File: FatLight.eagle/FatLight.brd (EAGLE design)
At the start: 75 x 100 mm, 27 parts, among them Q1 IRF540, Q2 IRF540, Q3 IRF540, Q4 16MHz, U1 ATMEGA328P-PU

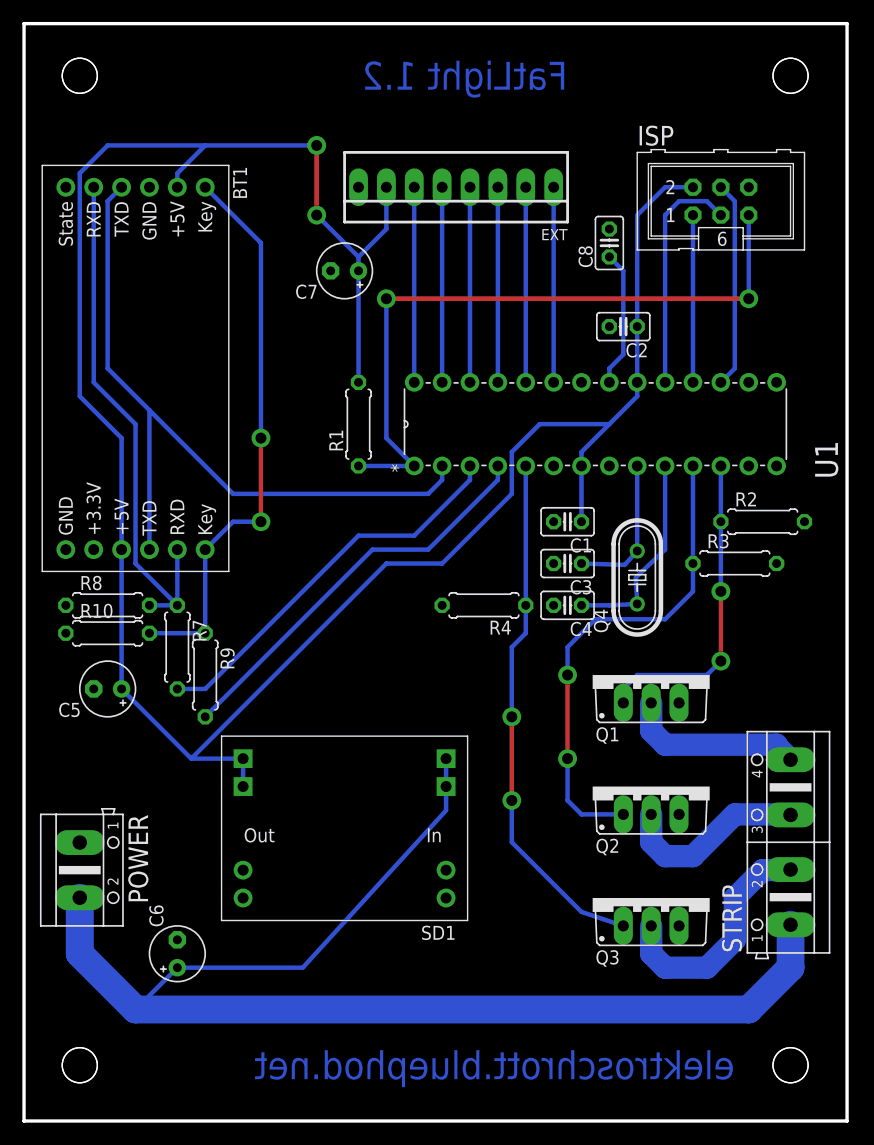
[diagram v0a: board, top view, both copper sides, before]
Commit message: Neue Board-Revision 1.3 mit stark optimiertem Layout und korrigiertem BT-Pinout
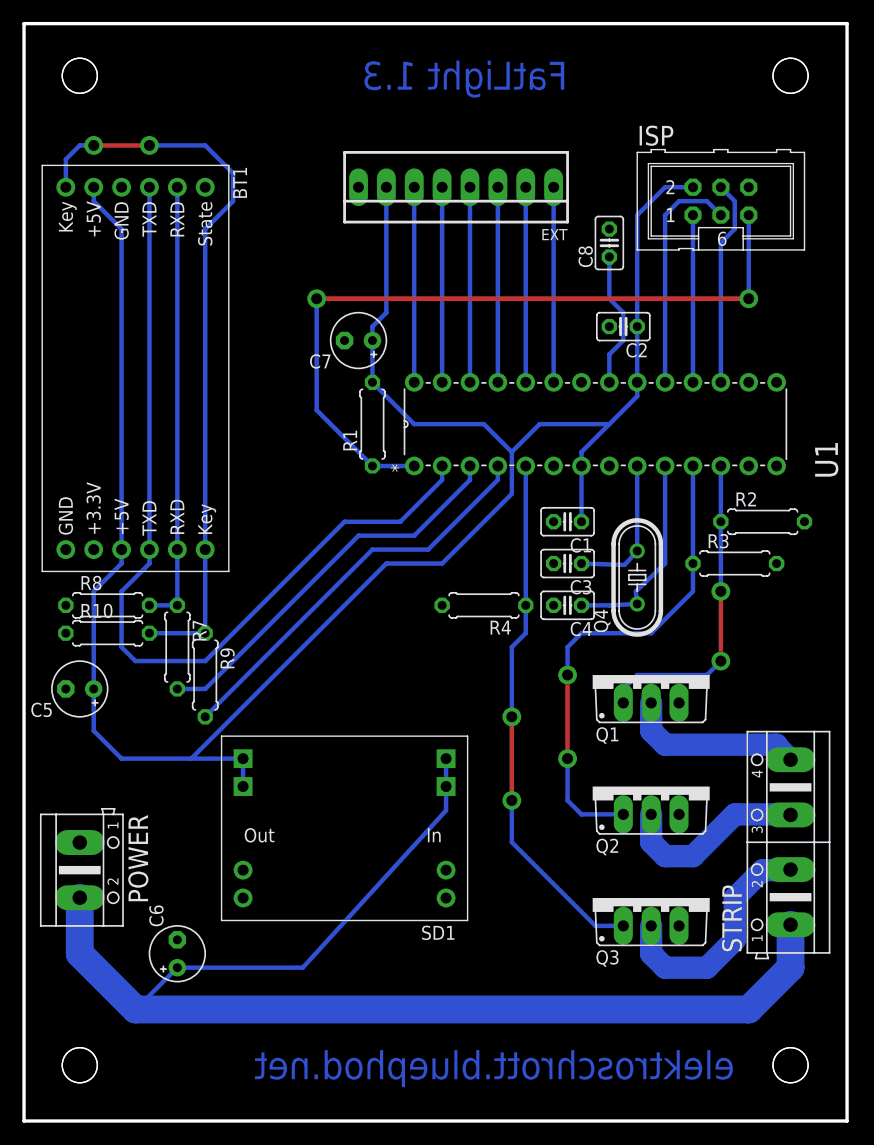
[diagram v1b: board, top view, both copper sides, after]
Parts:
- moved C7 6.48 mm to (30.5, 71.1)
- moved C5 2.54 mm to (5.08, 39.4)
- moved R1 1.27 mm to (31.8, 63.5)
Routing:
- net +5V: track 212.0 -> 191.6 mm, vias 2 -> 0
- net N$3: track 51.4 -> 67.4 mm
- net RXD_MCU: track 66.7 -> 80.8 mm
- net N$4: track 48.9 -> 40.6 mm
- net RESET: track 62.0 -> 68.1 mm
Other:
- board text added: "FatLight 1.3"
- board text removed: "FatLight 1.2"

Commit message: Bestückungsdruck verbessert
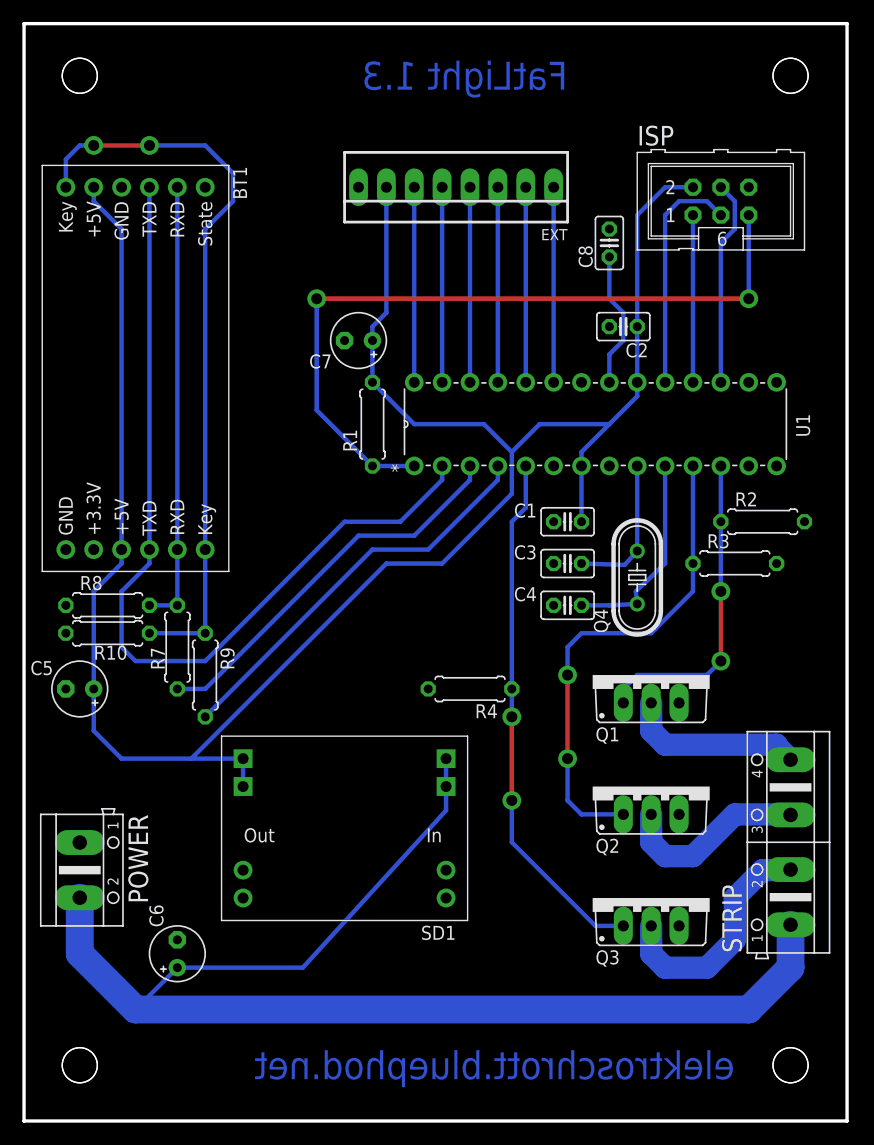
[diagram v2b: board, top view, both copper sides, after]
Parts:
- moved R4 7.73 mm to (40.6, 39.4)
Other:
- board text added: "+12/B/G/R"
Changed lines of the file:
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@@
 <text x="49.53" y="93.98" size="2.54" layer="16" font="vector" ratio="15" rot="MR0">FatLight 1.3</text>
 <text x="64.77" y="3.81" size="2.54" layer="16" font="vector" ratio="15" rot="MR0">elektroschrott.bluephod.net</text>
+<text x="65.405" y="24.765" size="1.27" layer="27" rot="R90">+12/B/G/R</text>
 </plain>
 <attributes>
@@
 </autorouter>
 <elements>
-<element name="BT1" library="ZAP-Wireless" package="HC-05-6PIN" value="BT-MODULE" x="10.16" y="68.58" rot="R270"/>
-<element name="C1" library="rcl" package="C025-025X050" value="100nF" x="49.53" y="54.61" rot="R180"/>
+<element name="BT1" library="ZAP-Wireless" package="HC-05-6PIN" value="BT-MODULE" x="10.16" y="68.58" smashed="yes" rot="R270">
+<attribute name="NAME" x="19.05" y="86.995" size="1.27" layer="21" rot="R270"/>
+<attribute name="VALUE" x="3.81" y="74.295" size="1.27" layer="27" rot="R270"/>
+</element>
+<element name="C1" library="rcl" package="C025-025X050" value="100nF" x="49.53" y="54.61" smashed="yes" rot="R180">
+<attribute name="NAME" x="46.736" y="56.261" size="1.27" layer="25" ratio="10" rot="R180"/>
+<attribute name="VALUE" x="46.736" y="54.864" size="1.27" layer="27" ratio="10" rot="R180"/>
+</element>
 <element name="C2" library="rcl" package="C025-025X050" value="100nF" x="54.61" y="72.39" rot="R180"/>
-<element name="C3" library="rcl" package="C025-025X050" value="22pF" x="49.53" y="50.8" rot="R180"/>
-<element name="C4" library="rcl" package="C025-025X050" value="22pF" x="49.53" y="46.99" rot="R180"/>
-<element name="C5" library="rcl" package="E2,5-5" value="100µF" x="5.08" y="39.37" rot="R180"/>
+<element name="C3" library="rcl" package="C025-025X050" value="22pF" x="49.53" y="50.8" smashed="yes" rot="R180">
+<attribute name="NAME" x="46.736" y="52.451" size="1.27" layer="25" ratio="10" rot="R180"/>
+<attribute name="VALUE" x="46.736" y="51.054" size="1.27" layer="27" ratio="10" rot="R180"/>
+</element>
+<element name="C4" library="rcl" package="C025-025X050" value="22pF" x="49.53" y="46.99" smashed="yes" rot="R180">
+<attribute name="NAME" x="46.736" y="48.641" size="1.27" layer="25" ratio="10" rot="R180"/>
+<attribute name="VALUE" x="46.736" y="47.244" size="1.27" layer="27" ratio="10" rot="R180"/>
+</element>
+<element name="C5" library="rcl" package="E2,5-5" value="100µF" x="5.08" y="39.37" smashed="yes" rot="R180">
+<attribute name="NAME" x="2.667" y="41.91" size="1.27" layer="25" ratio="10" rot="R180"/>
+<attribute name="VALUE" x="1.397" y="38.227" size="1.27" layer="27" ratio="10" rot="R270"/>
+</element>
 <element name="C6" library="rcl" package="E2,5-5" value="100µF" x="13.97" y="15.24" rot="R90"/>
 <element name="EXT" library="con-molex" package="22-23-2081" value="PSK-8" x="39.37" y="85.09" rot="R180">
@@
 </element>
 <element name="R1" library="rcl" package="0207/7" value="10k" x="31.75" y="63.5" rot="R90"/>
-<element name="R10" library="rcl" package="0207/7" value="20k" x="7.62" y="44.45"/>
+<element name="R10" library="rcl" package="0207/7" value="20k" x="7.62" y="44.45" smashed="yes">
+<attribute name="NAME" x="6.35" y="42.037" size="1.27" layer="25" ratio="10"/>
+<attribute name="VALUE" x="5.334" y="43.8912" size="1.27" layer="27" ratio="10"/>
+</element>
 <element name="R2" library="rcl" package="0207/7" value="10k" x="67.31" y="54.61"/>
 <element name="R3" library="rcl" package="0207/7" value="10k" x="64.77" y="50.8"/>
-<element name="R4" library="rcl" package="0207/7" value="10k" x="41.91" y="46.99" rot="R180"/>
-<element name="R7" library="rcl" package="0207/7" value="10k" x="13.97" y="43.18" rot="R270"/>
+<element name="R4" library="rcl" package="0207/7" value="10k" x="40.64" y="39.37" rot="R180"/>
+<element name="R7" library="rcl" package="0207/7" value="10k" x="13.97" y="43.18" smashed="yes" rot="R270">
+<attribute name="NAME" x="11.557" y="43.18" size="1.27" layer="25" ratio="10" rot="R270"/>
+<attribute name="VALUE" x="13.4112" y="45.466" size="1.27" layer="27" ratio="10" rot="R270"/>
+</element>
 <element name="R8" library="rcl" package="0207/7" value="20k" x="7.62" y="46.99"/>
 <element name="R9" library="rcl" package="0207/7" value="10k" x="16.51" y="40.64" rot="R270"/>
-<element name="SD1" library="Zap-Powerconverters" package="STEPDOWN-21X16" value="D-SUN-STEPDOWN" x="29.21" y="26.67" rot="R180"/>
-<element name="U1" library="Zap-Mikrocontroller" package="DIP254P762X457-28" value="ATMEGA328P-PU" x="68.58" y="67.31" rot="R90">
+<element name="SD1" library="Zap-Powerconverters" package="STEPDOWN-21X16" value="D-SUN-STEPDOWN" x="29.21" y="26.67" smashed="yes" rot="R180">
+<attribute name="NAME" x="39.37" y="17.78" size="1.27" layer="25" rot="R180"/>
+<attribute name="VALUE" x="37.465" y="28.575" size="1.27" layer="27" rot="R180"/>
+</element>
+<element name="U1" library="Zap-Mikrocontroller" package="DIP254P762X457-28" value="ATMEGA328P-PU" x="68.58" y="67.31" smashed="yes" rot="R90">
 <attribute name="PACKAGE" value="PDIP-28" x="68.58" y="67.31" size="1.778" layer="27" rot="R90" display="off"/>
 <attribute name="OC_NEWARK" value="15R0268" x="68.58" y="67.31" size="1.778" layer="27" rot="R90" display="off"/>
@@
 <attribute name="SUPPLIER" value="Atmel" x="68.58" y="67.31" size="1.778" layer="27" rot="R90" display="off"/>
 <attribute name="OC_FARNELL" value="1715487" x="68.58" y="67.31" size="1.778" layer="27" rot="R90" display="off"/>
+<attribute name="NAME" x="71.628" y="62.3062" size="1.27" layer="25" ratio="10" rot="SR90"/>
+<attribute name="VALUE" x="53.6956" y="61.595" size="1.27" layer="27" ratio="10" rot="SR0"/>
 </element>
 <element name="C7" library="rcl" package="E2,5-5" value="100µF" x="30.48" y="71.12" rot="R180"/>
-<element name="C8" library="rcl" package="C025-025X050" value="100nF" x="53.34" y="80.01" rot="R90"/>
+<element name="C8" library="rcl" package="C025-025X050" value="100nF" x="53.34" y="80.01" smashed="yes" rot="R90">
+<attribute name="NAME" x="51.816" y="77.724" size="1.27" layer="25" ratio="10" rot="R90"/>
+<attribute name="VALUE" x="54.864" y="82.804" size="1.27" layer="27" ratio="10" rot="R90"/>
+</element>
 <element name="STRIP" library="con-ptr500" package="AK500/4" value="" x="69.85" y="25.4" rot="R90">
 <attribute name="OC_NEWARK" value="unknown" x="69.85" y="25.4" size="1.778" layer="27" rot="R90" display="off"/>
@@
 <contactref element="R4" pad="1"/>
 <contactref element="U1" pad="5"/>
-<wire x1="45.72" y1="59.69" x2="45.72" y2="46.99" width="0.4064" layer="16"/>
 <wire x1="54.61" y1="17.78" x2="52.07" y2="17.78" width="0.4064" layer="16"/>
 <wire x1="52.07" y1="17.78" x2="44.45" y2="25.4" width="0.4064" layer="16"/>
@@
 <via x="44.45" y="29.21" extent="1-16" drill="1"/>
 <wire x1="44.45" y1="29.21" x2="44.45" y2="25.4" width="0.4064" layer="16"/>
-<wire x1="45.72" y1="46.99" x2="45.72" y2="44.45" width="0.4064" layer="16"/>
-<wire x1="45.72" y1="44.45" x2="44.45" y2="43.18" width="0.4064" layer="16"/>
-<wire x1="44.45" y1="43.18" x2="44.45" y2="36.83" width="0.4064" layer="16"/>
+<wire x1="44.45" y1="36.83" x2="44.45" y2="39.37" width="0.4064" layer="16"/>
+<wire x1="44.45" y1="39.37" x2="44.45" y2="54.61" width="0.4064" layer="16"/>
+<wire x1="44.45" y1="54.61" x2="45.72" y2="55.88" width="0.4064" layer="16"/>
+<wire x1="45.72" y1="55.88" x2="45.72" y2="59.69" width="0.4064" layer="16"/>
 </signal>
 <signal name="SCK">
